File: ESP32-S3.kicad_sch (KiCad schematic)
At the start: 29 parts, among them J1 Speaker, SW1 Reset, SW2 Boot, SW3 Down, SW4 User, SW5 Up, U1 SHT4x, U2 ESP32-S3-MINI-1, U3 MAX98357A

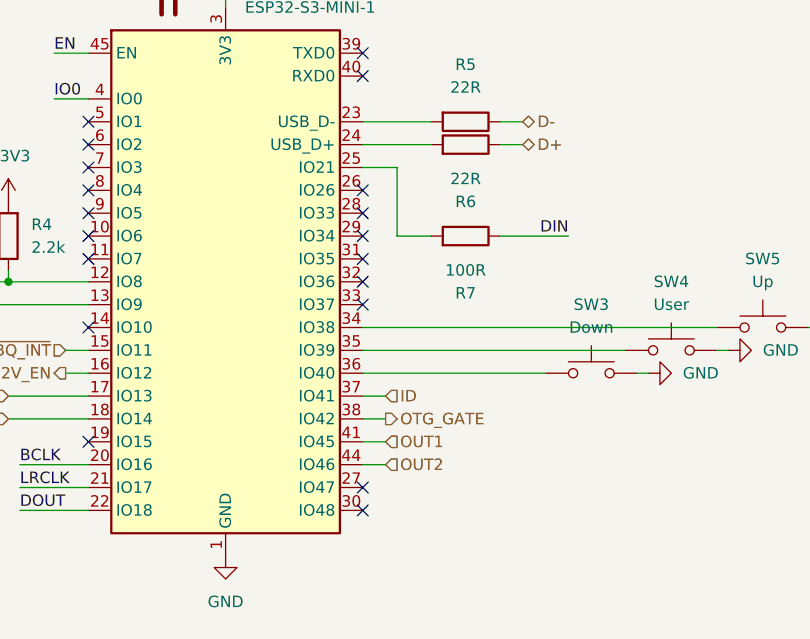
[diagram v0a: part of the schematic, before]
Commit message: Group power components
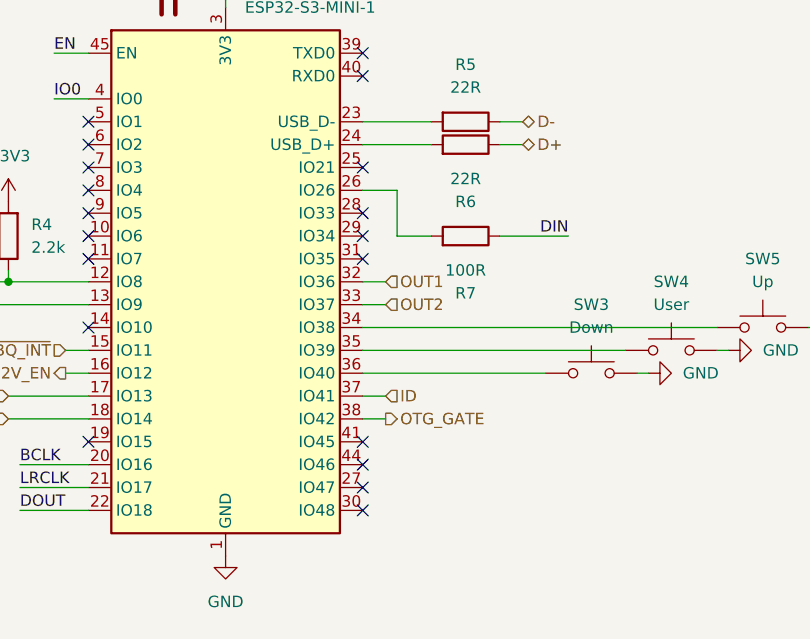
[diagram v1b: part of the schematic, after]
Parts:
- SW1, SW2: footprint Button_Switch_THT:SW_PUSH_6mm -> Button_Switch_SMD:SW_SPST_Omron_B3FS-100xP
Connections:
- net OUT1: now also U2.32 (IO36); no longer U2.41 (IO45)
- net OUT2: now also U2.33 (IO37); no longer U2.44 (IO46)
- net at U2.25 (IO21): no longer R7.2
- net at U2.26 (IO26): now also R7.2
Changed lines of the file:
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@@
 	)
 	(no_connect
+		(at 119.38 88.9)
+	)
+	(no_connect
 		(at 88.9 86.36)
 	)
@@
 	)
 	(no_connect
-		(at 88.9 55.88)
+		(at 119.38 55.88)
 	)
 	(no_connect
-		(at 119.38 68.58)
+		(at 88.9 55.88)
 	)
 	(no_connect
@@
 	)
 	(no_connect
-		(at 119.38 71.12)
-	)
-	(no_connect
 		(at 119.38 45.72)
 	)
@@
 	)
 	(no_connect
-		(at 119.38 58.42)
+		(at 88.9 53.34)
 	)
 	(no_connect
-		(at 88.9 53.34)
+		(at 119.38 86.36)
 	)
 	(wire
@@
 	(wire
 		(pts
-			(xy 123.19 63.5) (xy 123.19 55.88)
+			(xy 123.19 63.5) (xy 123.19 58.42)
 		)
 		(stroke
@@
 	(wire
 		(pts
-			(xy 123.19 55.88) (xy 119.38 55.88)
+			(xy 121.92 68.58) (xy 119.38 68.58)
 		)
 		(stroke
@@
 	(wire
 		(pts
+			(xy 119.38 58.42) (xy 123.19 58.42)
+		)
+		(stroke
+			(width 0)
+			(type default)
+		)
+	)
+	(wire
+		(pts
 			(xy 36.83 31.75) (xy 34.29 31.75)
 		)
@@
 	(wire
 		(pts
-			(xy 121.92 86.36) (xy 119.38 86.36)
-		)
-		(stroke
-			(width 0)
-			(type default)
-		)
-	)
-	(wire
-		(pts
 			(xy 201.93 97.79) (xy 215.9 97.79)
 		)
@@
 	(wire
 		(pts
+			(xy 121.92 71.12) (xy 119.38 71.12)
+		)
+		(stroke
+			(width 0)
+			(type default)
+		)
+	)
+	(wire
+		(pts
 			(xy 119.38 76.2) (xy 148.59 76.2)
 		)
@@
 	(wire
 		(pts
-			(xy 121.92 88.9) (xy 119.38 88.9)
-		)
-		(stroke
-			(width 0)
-			(type default)
-		)
-	)
-	(wire
-		(pts
 			(xy 71.12 71.12) (xy 88.9 71.12)
 		)
@@
 		)
 	)
-	(hierarchical_label "ID"
+	(hierarchical_label "OUT2"
 		(shape input)
-		(at 121.92 81.28 0)
+		(at 121.92 71.12 0)
 		(effects
 			(font
@@
 		)
 	)
-	(hierarchical_label "OUT1"
+	(hierarchical_label "ID"
 		(shape input)
-		(at 121.92 86.36 0)
+		(at 121.92 81.28 0)
 		(effects
 			(font
@@
 		)
 	)
-	(hierarchical_label "OUT2"
+	(hierarchical_label "FAN_GATE"
 		(shape input)
-		(at 121.92 88.9 0)
+		(at 80.01 81.28 180)
 		(effects
 			(font
 				(size 1.27 1.27)
 			)
-			(justify left)
+			(justify right)
 		)
 	)
-	(hierarchical_label "FAN_GATE"
+	(hierarchical_label "OUT1"
 		(shape input)
-		(at 80.01 81.28 180)
+		(at 121.92 68.58 0)
 		(effects
 			(font
 				(size 1.27 1.27)
 			)
-			(justify right)
+			(justify left)
 		)
 	)
@@
 			)
 		)
-		(property "Footprint" "Button_Switch_THT:SW_PUSH_6mm"
+		(property "Footprint" "Button_Switch_SMD:SW_SPST_Omron_B3FS-100xP"
 			(at 19.05 36.83 0)
 			(hide yes)
@@
 			)
 		)
-		(property "Footprint" "Button_Switch_THT:SW_PUSH_6mm"
+		(property "Footprint" "Button_Switch_SMD:SW_SPST_Omron_B3FS-100xP"
 			(at 46.99 36.83 0)
 			(hide yes)

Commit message: Fully routed, no DRC errors
tysm Kevin :D
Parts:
- C2, C4, C5: footprint Capacitor_SMD:C_0603_1608Metric -> Capacitor_SMD:C_0402_1005Metric
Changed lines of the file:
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@@
 			)
 		)
-		(property "Footprint" "Capacitor_SMD:C_0603_1608Metric"
+		(property "Footprint" "Capacitor_SMD:C_0402_1005Metric"
 			(at 93.6752 138.43 0)
 			(hide yes)
@@
 			)
 		)
-		(property "Footprint" "Capacitor_SMD:C_0603_1608Metric"
+		(property "Footprint" "Capacitor_SMD:C_0402_1005Metric"
 			(at 30.1752 138.43 0)
 			(hide yes)
@@
 			)
 		)
-		(property "Footprint" "Capacitor_SMD:C_0603_1608Metric"
+		(property "Footprint" "Capacitor_SMD:C_0402_1005Metric"
 			(at 61.9252 138.43 0)
 			(hide yes)

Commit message: Fixed DOUT short circuit
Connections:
- net DOUT: no longer D3.1 (DOUT)
- no-connect marks 19 -> 20
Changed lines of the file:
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@@
+	)
+	(no_connect
+		(at 110.49 147.32)
 	)
 	(no_connect
@@
 		(pts
 			(xy 119.38 76.2) (xy 148.59 76.2)
-		)
-		(stroke
-			(width 0)
-			(type default)
-		)
-	)
-	(wire
-		(pts
-			(xy 115.57 147.32) (xy 110.49 147.32)
 		)
 		(stroke
@@
 		)
 	)
-	(label "DOUT"
-		(at 115.57 147.32 180)
-		(effects
-			(font
-				(size 1.27 1.27)
-			)
-			(justify right bottom)
-		)
-	)

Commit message: Fix more bugs
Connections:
- net EN: now also C1.1
- net GND: now also SW1.1
- net OTG: now reaches U2.41 (IO45)
- no-connect marks 20 -> 19
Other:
- moved on the sheet: C1, R1

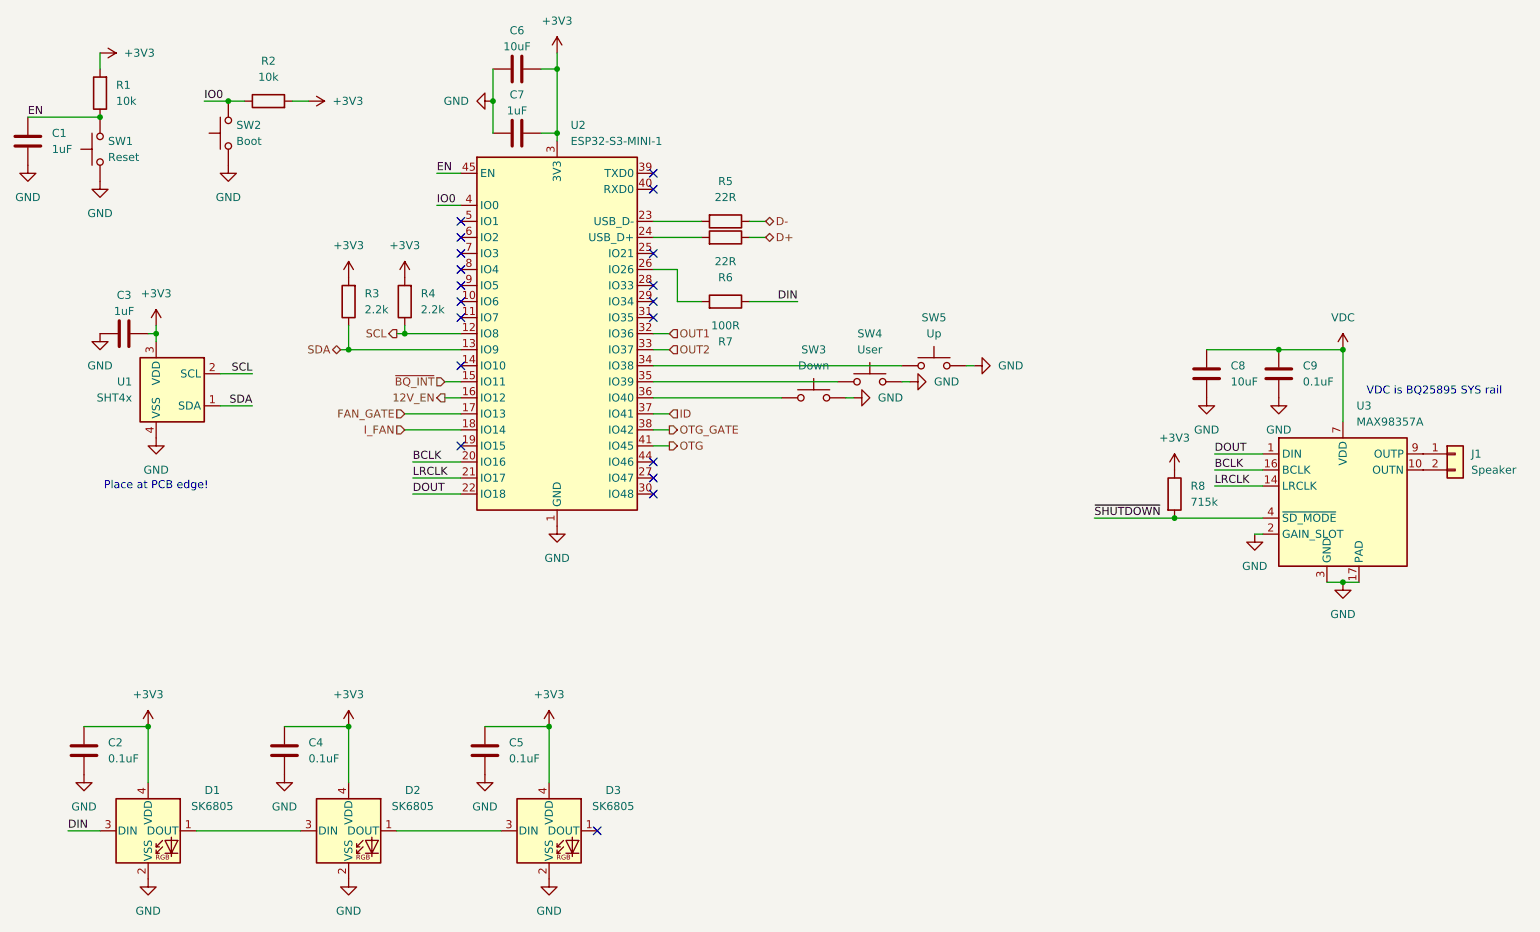
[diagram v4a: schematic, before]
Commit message: Finalize routed Cryobelt PCB for fabrication
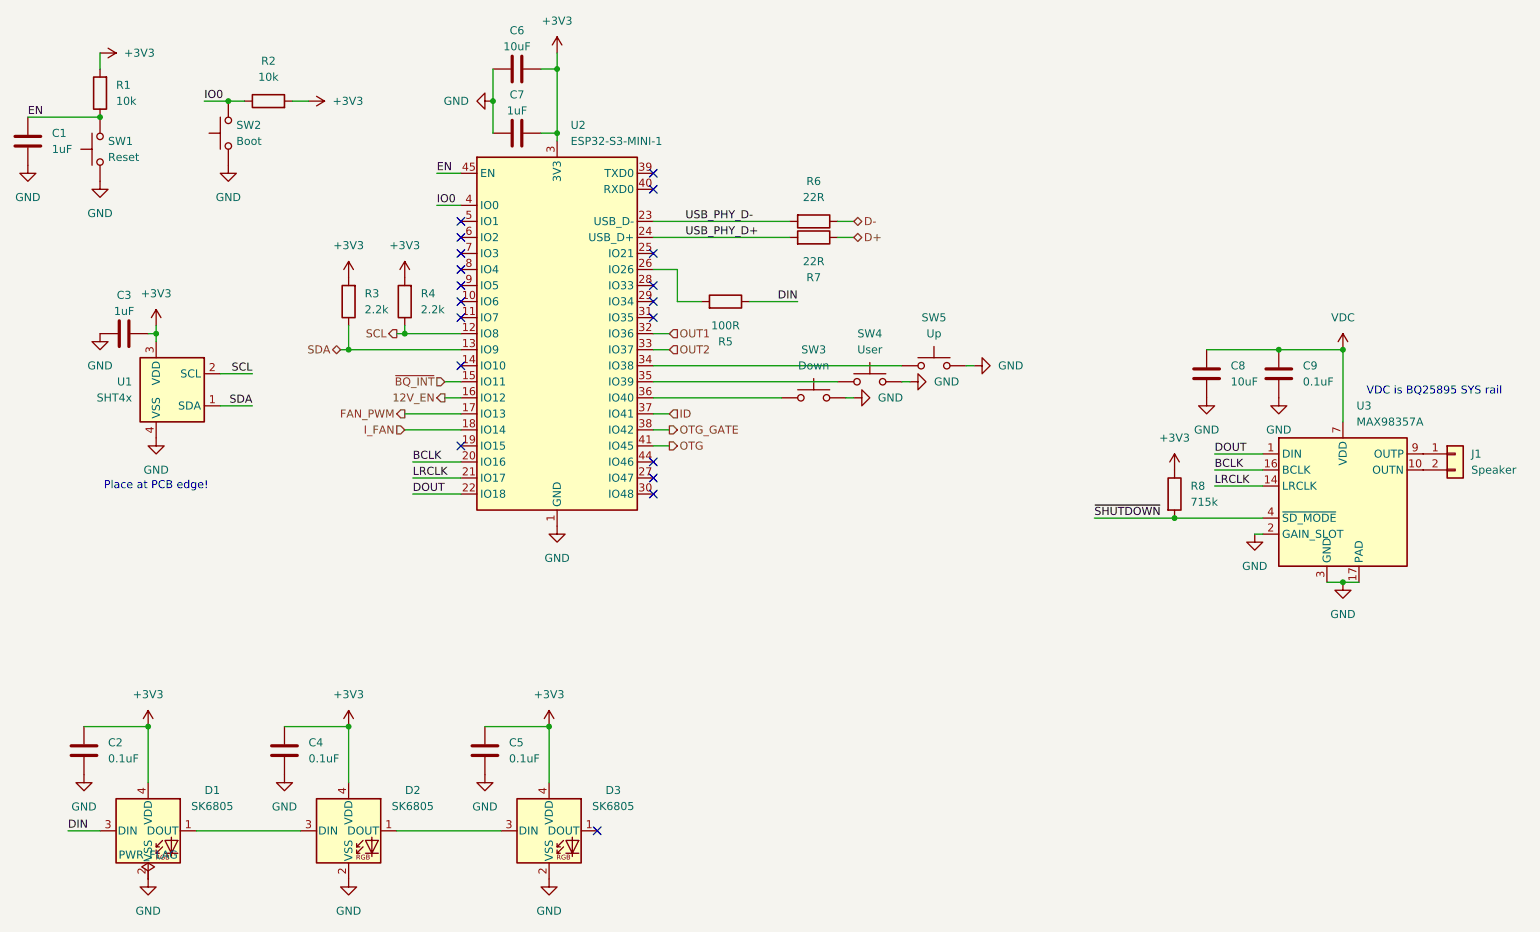
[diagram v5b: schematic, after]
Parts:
- C1, C3, C7: LCSC Part # (none) -> C86012; MPN (none) -> GRM188R61A105KA61D; Manufacturer (none) -> Murata
- C2, C4, C5: LCSC Part # (none) -> C60474; MPN (none) -> CC0402KRX7R7BB104; Manufacturer (none) -> YAGEO
- C6, C8: LCSC Part # (none) -> C703114; MPN (none) -> GRM188R61A106KAALD; Manufacturer (none) -> Murata
- C9: LCSC Part # (none) -> C14663; MPN (none) -> CC0603KRX7R9BB104; Manufacturer (none) -> YAGEO
- D1, D2, D3: LCSC Part # (none) -> C2909056; MPN (none) -> SK6805MICRO-J; Manufacturer (none) -> OPSCO Optoelectronics
- J1: footprint Connector_Wire:SolderWire-0.5sqmm_1x02_P4.6mm_D0.9mm_OD2.1mm -> Connector_Wire:SolderWire-0.1sqmm_1x02_P3.6mm_D0.4mm_OD1mm
- R1, R2: LCSC Part # (none) -> C98220; MPN (none) -> RC0603FR-0710KL; Manufacturer (none) -> YAGEO
- R3, R4: LCSC Part # (none) -> C4190; MPN (none) -> 0603WAF2201T5E; Manufacturer (none) -> UNI-ROYAL
- R5: renamed from R7; LCSC Part # (none) -> C22775; MPN (none) -> 0603WAF1000T5E; Manufacturer (none) -> UNI-ROYAL
- R6: renamed from R5; LCSC Part # (none) -> C23345; MPN (none) -> 0603WAF220JT5E; Manufacturer (none) -> UNI-ROYAL
- R7: renamed from R6; LCSC Part # (none) -> C23345; MPN (none) -> 0603WAF220JT5E; Manufacturer (none) -> UNI-ROYAL
- R8: LCSC Part # (none) -> C137685; MPN (none) -> RC0603FR-07715KL; Manufacturer (none) -> YAGEO
- SW1, SW2: LCSC Part # (none) -> C271750; MPN (none) -> B3FS-1000P; Manufacturer (none) -> Omron
- SW3, SW4, SW5: footprint PG1316:PG1316S -> Cryobelt:PG1316S
- U1: LCSC Part # (none) -> C2909890; MPN (none) -> SHT40-AD1B-R2; Manufacturer (none) -> Sensirion
- U2: footprint RF_Module:ESP32-S2-MINI-1 -> Cryobelt:ESP32-S3-MINI-1; symbol RF_Module:ESP32-S3-MINI-1 -> Cryobelt_ESP32:ESP32-S3-MINI-1; LCSC Part # (none) -> C2913206; MPN (none) -> ESP32-S3-MINI-1-N8; Manufacturer (none) -> Espressif Systems
- U3: symbol Audio:MAX98357A -> Cryobelt_Audio:MAX98357A; LCSC Part # (none) -> C910544; MPN (none) -> MAX98357AETE+T; Manufacturer (none) -> Analog Devices / Maxim
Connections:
- net USB_PHY_D-: now reaches R6.2, U2.23 (USB_D-)
- net USB_PHY_D+: now reaches R7.2, U2.24 (USB_D+)
- net FAN_GATE renamed FAN_PWM
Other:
- moved on the sheet: R6, R7

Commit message: Replace SK6805 LEDs with 3.3V WS2812B
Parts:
- D1, D2, D3: value SK6805 -> WS2812B-2427-V6; footprint LED_SMD:LED_SK6805_PLCC4_2.4x2.7mm_P1.3mm -> Cryobelt:WS2812B-2427-V6_Rotated180; LCSC Part # C2909056 -> C52941389; MPN SK6805MICRO-J -> WS2812B-2427-V6; Manufacturer OPSCO Optoelectronics -> Worldsemi
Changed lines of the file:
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@@
 			)
 		)
-		(property "Value" "SK6805"
+		(property "Value" "WS2812B-2427-V6"
 			(at 81.28 143.4398 0)
 			(show_name no)
@@
 			)
 		)
-		(property "Footprint" "LED_SMD:LED_SK6805_PLCC4_2.4x2.7mm_P1.3mm"
+		(property "Footprint" "Cryobelt:WS2812B-2427-V6_Rotated180"
 			(at 72.39 154.94 0)
 			(hide yes)
@@
 			)
 		)
-		(property "Datasheet" "https://cdn-shop.adafruit.com/product-files/3484/3484_Datasheet.pdf"
+		(property "Datasheet" "https://atta.szlcsc.com/upload/public/pdf/source/20251224/E1A9CA691775549EA7D4A013FE234DF1.pdf"
 			(at 73.66 156.845 0)
 			(hide yes)
@@
 			)
 		)
-		(property "Description" "RGB LED with integrated controller"
+		(property "Description" "3.3 V compatible addressable RGB LED; 24-bit 800 kbit/s; footprint remapped for 180 degree substitution"
 			(at 71.12 147.32 0)
 			(hide yes)
@@
 			)
 		)
-		(property "Manufacturer" "OPSCO Optoelectronics"
-			(at 0 0 0)
-			(hide yes)
-			(show_name no)
-			(do_not_autoplace no)
-			(effects
-				(font
-					(size 1.27 1.27)
-				)
-			)
-		)
-		(property "MPN" "SK6805MICRO-J"
-			(at 0 0 0)
-			(hide yes)
-			(show_name no)
-			(do_not_autoplace no)
-			(effects
-				(font
-					(size 1.27 1.27)
-				)
-			)
-		)
-		(property "LCSC Part #" "C2909056"
+		(property "Manufacturer" "Worldsemi"
+			(at 0 0 0)
+			(hide yes)
+			(show_name no)
+			(do_not_autoplace no)
+			(effects
+				(font
+					(size 1.27 1.27)
+				)
+			)
+		)
+		(property "MPN" "WS2812B-2427-V6"
+			(at 0 0 0)
+			(hide yes)
+			(show_name no)
+			(do_not_autoplace no)
+			(effects
+				(font
+					(size 1.27 1.27)
+				)
+			)
+		)
+		(property "LCSC Part #" "C52941389"
 			(at 0 0 0)
 			(hide yes)
@@
 			)
 		)
-		(property "Value" "SK6805"
+		(property "Value" "WS2812B-2427-V6"
 			(at 113.03 143.4398 0)
 			(show_name no)
@@
 			)
 		)
-		(property "Footprint" "LED_SMD:LED_SK6805_PLCC4_2.4x2.7mm_P1.3mm"
+		(property "Footprint" "Cryobelt:WS2812B-2427-V6_Rotated180"
 			(at 104.14 154.94 0)
 			(hide yes)
@@
 			)
 		)
-		(property "Datasheet" "https://cdn-shop.adafruit.com/product-files/3484/3484_Datasheet.pdf"
+		(property "Datasheet" "https://atta.szlcsc.com/upload/public/pdf/source/20251224/E1A9CA691775549EA7D4A013FE234DF1.pdf"
 			(at 105.41 156.845 0)
 			(hide yes)
@@
 			)
 		)
-		(property "Description" "RGB LED with integrated controller"
+		(property "Description" "3.3 V compatible addressable RGB LED; 24-bit 800 kbit/s; footprint remapped for 180 degree substitution"
 			(at 102.87 147.32 0)
 			(hide yes)
@@
 			)
 		)
-		(property "Manufacturer" "OPSCO Optoelectronics"
-			(at 0 0 0)
-			(hide yes)
-			(show_name no)
-			(do_not_autoplace no)
-			(effects
-				(font
-					(size 1.27 1.27)
-				)
-			)
-		)
-		(property "MPN" "SK6805MICRO-J"
-			(at 0 0 0)
-			(hide yes)
-			(show_name no)
-			(do_not_autoplace no)
-			(effects
-				(font
-					(size 1.27 1.27)
-				)
-			)
-		)
-		(property "LCSC Part #" "C2909056"
+		(property "Manufacturer" "Worldsemi"
+			(at 0 0 0)
+			(hide yes)
+			(show_name no)
+			(do_not_autoplace no)
+			(effects
+				(font
+					(size 1.27 1.27)
+				)
+			)
+		)
+		(property "MPN" "WS2812B-2427-V6"
+			(at 0 0 0)
+			(hide yes)
+			(show_name no)
+			(do_not_autoplace no)
+			(effects
+				(font
+					(size 1.27 1.27)
+				)
+			)
+		)
+		(property "LCSC Part #" "C52941389"
 			(at 0 0 0)
 			(hide yes)
@@
 			)
 		)
-		(property "Value" "SK6805"
+		(property "Value" "WS2812B-2427-V6"
 			(at 49.53 143.4398 0)
 			(show_name no)
@@
 			)
 		)
-		(property "Footprint" "LED_SMD:LED_SK6805_PLCC4_2.4x2.7mm_P1.3mm"
+		(property "Footprint" "Cryobelt:WS2812B-2427-V6_Rotated180"
 			(at 40.64 154.94 0)
 			(hide yes)
@@
 			)
 		)
-		(property "Datasheet" "https://cdn-shop.adafruit.com/product-files/3484/3484_Datasheet.pdf"
+		(property "Datasheet" "https://atta.szlcsc.com/upload/public/pdf/source/20251224/E1A9CA691775549EA7D4A013FE234DF1.pdf"
 			(at 41.91 156.845 0)
 			(hide yes)
@@
 			)
 		)
-		(property "Description" "RGB LED with integrated controller"
+		(property "Description" "3.3 V compatible addressable RGB LED; 24-bit 800 kbit/s; footprint remapped for 180 degree substitution"
 			(at 39.37 147.32 0)
 			(hide yes)
@@
 			)
 		)
-		(property "Manufacturer" "OPSCO Optoelectronics"
-			(at 0 0 0)
-			(hide yes)
-			(show_name no)
-			(do_not_autoplace no)
-			(effects
-				(font
-					(size 1.27 1.27)
-				)
-			)
-		)
-		(property "MPN" "SK6805MICRO-J"
-			(at 0 0 0)
-			(hide yes)
-			(show_name no)
-			(do_not_autoplace no)
-			(effects
-				(font
-					(size 1.27 1.27)
-				)
-			)
-		)
-		(property "LCSC Part #" "C2909056"
-			(at 0 0 0)
-			(hide yes)
+		(property "Manufacturer" "Worldsemi"
+			(at 0 0 0)
+			(hide yes)
+			(show_name no)
+			(do_not_autoplace no)
+			(effects
+				(font
+					(size 1.27 1.27)
+				)
+			)
+		)
+		(property "MPN" "WS2812B-2427-V6"
+			(at 0 0 0)
+			(hide yes)
+			(show_name no)
+			(do_not_autoplace no)
+			(effects
+				(font
+					(size 1.27 1.27)
+				)
+			)
+		)
+		(property "LCSC Part #" "C52941389"
+			(at 0 0 0)
+			(hide yes)

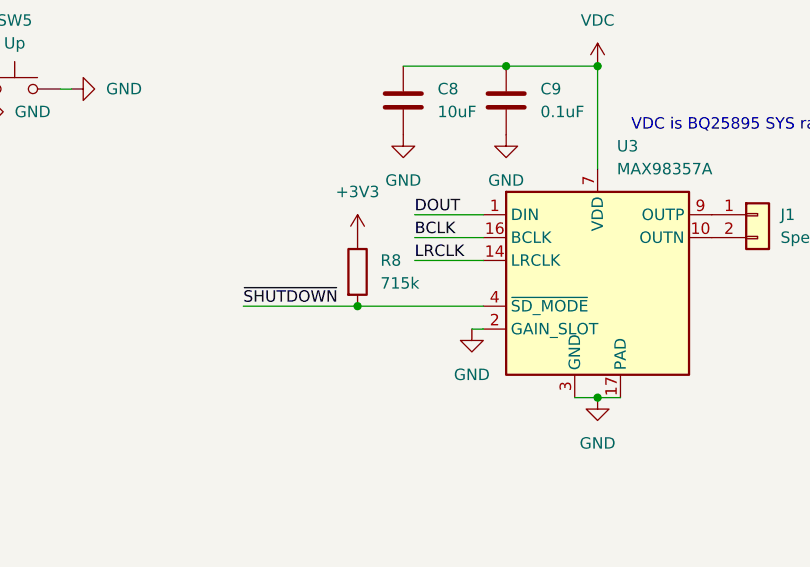
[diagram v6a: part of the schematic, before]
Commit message: Correct charger bootstrap and audio mode values
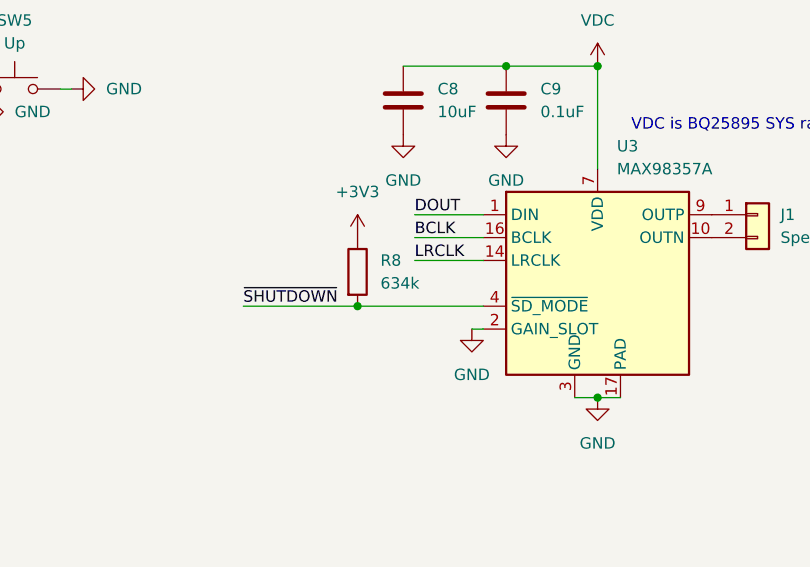
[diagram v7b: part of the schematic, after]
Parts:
- R8: value 715k -> 634k; LCSC Part # C137685 -> C273753; MPN RC0603FR-07715KL -> RC0603FR-07634KL
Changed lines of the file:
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@@
 			)
 		)
-		(property "Value" "715k"
+		(property "Value" "634k"
 			(at 204.47 95.2499 0)
 			(show_name no)
@@
 			)
 		)
-		(property "Datasheet" ""
+		(property "Datasheet" "https://www.lcsc.com/product-detail/C273753.html"
 			(at 201.93 93.98 0)
 			(hide yes)
@@
 			)
 		)
-		(property "Description" "Resistor"
+		(property "Description" "634 kOhm 1% SD_MODE pull-up for summed-mono selection at 3.3 V"
 			(at 201.93 93.98 0)
 			(hide yes)
@@
 			)
 		)
-		(property "MPN" "RC0603FR-07715KL"
+		(property "MPN" "RC0603FR-07634KL"
 			(at 0 0 0)
 			(hide yes)
@@
 			)
 		)
-		(property "LCSC Part #" "C137685"
+		(property "LCSC Part #" "C273753"
 			(at 0 0 0)
 			(hide yes)
